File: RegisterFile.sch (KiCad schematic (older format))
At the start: 8 parts, among them U44 IDT71342LA20JG, U45 IDT71342LA20JG, U46 IDT71342LA20JG, U47 IDT71342LA20JG

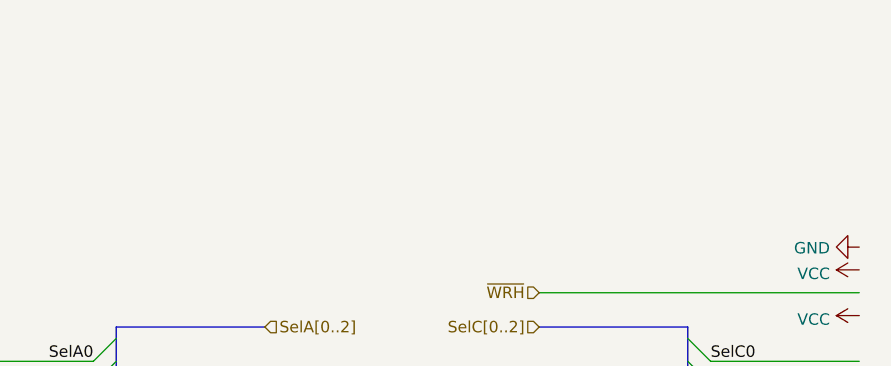
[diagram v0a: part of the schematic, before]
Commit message: Latch the A and B values between ID and EX stages.
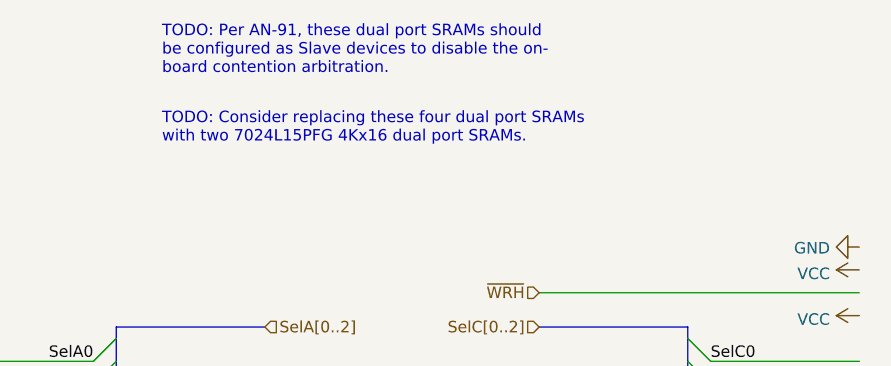
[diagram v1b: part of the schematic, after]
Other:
- note added: "TODO: Consider replacing these four dual port SRAMs\nwith two 7024L15PFG 4Kx16 dual port SRAMs."
- note added: "TODO: Per AN-91, these dual port SRAMs should\nbe configured as Slave devices to disable the on-\nboard contention arbitration."
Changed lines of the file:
@@
 $Descr A2 23386 16535
 encoding utf-8
-Sheet 5 32
+Sheet 4 34
 Title "Register File"
 Date ""
@@
 Text Label 12200 7300 0    50   ~ 0
 C15
+Text Notes 10200 4050 0    50   ~ 0
+TODO: Per AN-91, these dual port SRAMs should\nbe configured as Slave devices to disable the on-\nboard contention arbitration.
+Text Notes 10200 4350 0    50   ~ 0
+TODO: Consider replacing these four dual port SRAMs\nwith two 7024L15PFG 4Kx16 dual port SRAMs.
 Wire Bus Line
 	7100 5150 7100 5400

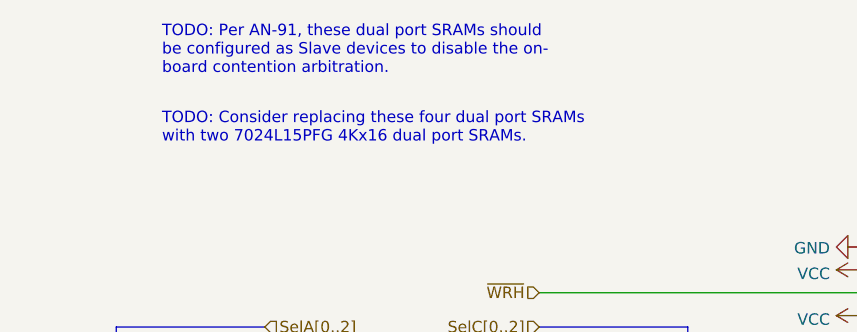
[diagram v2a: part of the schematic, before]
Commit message: Instruction Memory RAM ICs are slave devices.
Per AN-91, the dual port SRAMs in IF should be configured as Slave devices
to disable the on-board contention arbitration. We accept invalid results
during simultaneous access to individual memory cells in return for the
simplicity of not needing to handle the busy signal.
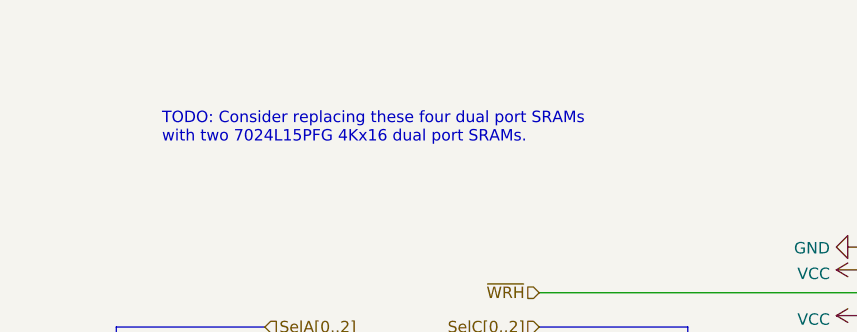
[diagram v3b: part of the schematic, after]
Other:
- note removed: "TODO: Per AN-91, these dual port SRAMs should\nbe configured as Slave devices to disable the on-\nboard contention arbitration."
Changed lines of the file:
@@
 Text Label 12200 7300 0    50   ~ 0
 C15
-Text Notes 10200 4050 0    50   ~ 0
-TODO: Per AN-91, these dual port SRAMs should\nbe configured as Slave devices to disable the on-\nboard contention arbitration.
 Text Notes 10200 4350 0    50   ~ 0
 TODO: Consider replacing these four dual port SRAMs\nwith two 7024L15PFG 4Kx16 dual port SRAMs.

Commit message: Use IDT 7024L15PFG dual port SRAM for the register file.
These are smaller and faster than the ICs I was using before, and I only
need two of them.
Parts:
- removed C50, C51: 100nF, Capacitor_SMD:C_0603_1608Metric_Pad1.08x0.95mm_HandSolder, symbol Device:C
- removed U44, U45, U46, U47: IDT71342LA20JG, Package_LCC:PLCC-52_SMD-Socket, symbol MainBoard-rescue:IDT71342LA20JG-Memory_RAM
- added U10, U9: IDT7024L15PFG, Package_QFP:TQFP-100_14x14mm_P0.5mm, symbol Memory_RAM:IDT7024L15PFG
- renumbered C48 to C14, C49 to C15
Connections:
- wire segments 102 -> 118
- no-connect marks 0 -> 4
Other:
- note added: "Both dual port SRAMs are configured in Slave mode. This disables the\non board contention arbitration logic. Per application note, AN-91, a\nsimultaneous read and write to the same cell will flow through from one\nport to another after a short delay."
- note removed: "TODO: Consider replacing these four dual port SRAMs\nwith two 7024L15PFG 4Kx16 dual port SRAMs."
- moved on the sheet: C14, C15

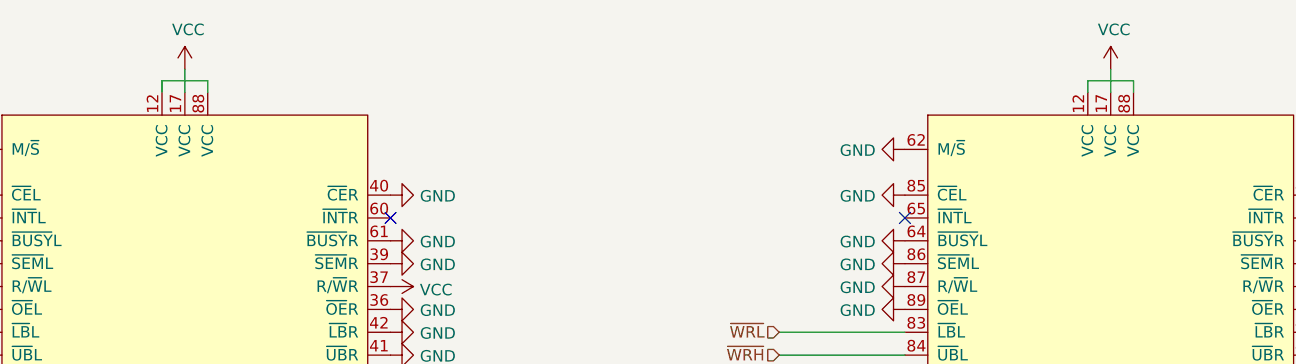
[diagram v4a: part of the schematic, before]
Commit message: Fix ERC errors and change operands in EX.
Now, A is the left operand and B is the right operand. The immediate
value may be selected for the right hand operand.
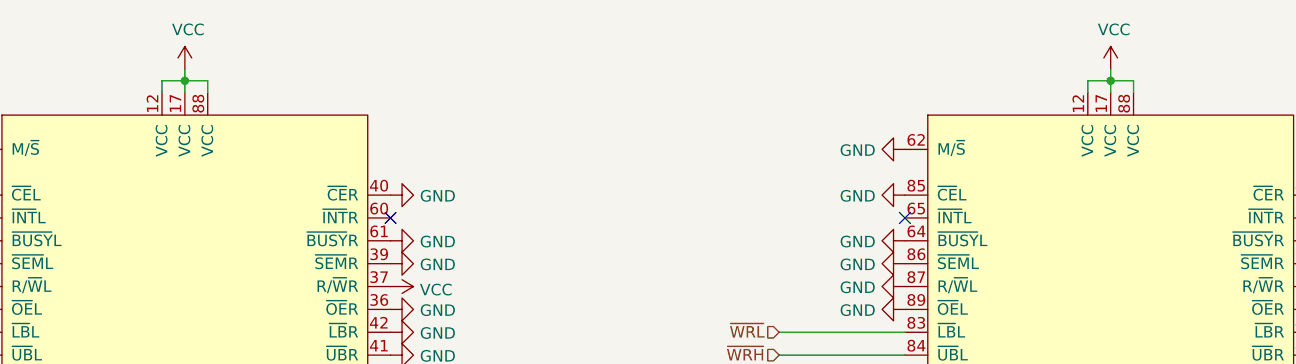
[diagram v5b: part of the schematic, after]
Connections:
- net VCC: now also U10.12 (VCC), U10.88 (VCC), U9.12 (VCC), U9.88 (VCC)
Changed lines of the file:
@@
 $EndComp
 Wire Wire Line
-	3350 1650 3350 1600
-Wire Wire Line
-	3350 1600 3550 1600
+	3350 1600 3450 1600
 Wire Wire Line
 	3550 1600 3550 1650
-Wire Wire Line
-	3450 1650 3450 1550
 $Comp
 L power:VCC #PWR062
@@
 $EndComp
 Wire Wire Line
-	7400 1650 7400 1600
-Wire Wire Line
-	7400 1600 7600 1600
+	7400 1600 7500 1600
 Wire Wire Line
 	7600 1600 7600 1650
-Wire Wire Line
-	7500 1650 7500 1550
 $Comp
 L power:VCC #PWR095
@@
 	0    -1   1    0
 $EndComp
-Wire Bus Line
-	2150 2900 2150 3100
-Wire Bus Line
-	4750 2900 4750 3100
-Wire Bus Line
-	6200 2900 6200 3100
-Wire Bus Line
-	8800 2900 8800 3100
-Wire Bus Line
-	2150 4200 2150 5700
-Wire Bus Line
-	4750 4200 4750 5700
-Wire Bus Line
-	6200 4200 6200 5700
-Wire Bus Line
-	8800 4200 8800 5700
 Text Notes 2550 7250 0    50   ~ 0
 Both dual port SRAMs are configured in Slave mode. This disables the\non board contention arbitration logic. Per application note, AN-91, a\nsimultaneous read and write to the same cell will flow through from one\nport to another after a short delay.
+Wire Wire Line
+	3350 1650 3350 1600
+Wire Wire Line
+	7400 1650 7400 1600
+Wire Wire Line
+	7500 1550 7500 1600
+Connection ~ 7500 1600
+Wire Wire Line
+	7500 1600 7600 1600
+Wire Wire Line
+	7500 1600 7500 1650
+Wire Wire Line
+	3450 1550 3450 1600
+Connection ~ 3450 1600
+Wire Wire Line
+	3450 1600 3550 1600
+Wire Wire Line
+	3450 1600 3450 1650
+Wire Bus Line
+	2150 2900 2150 3100
+Wire Bus Line
+	4750 2900 4750 3100
+Wire Bus Line
+	6200 2900 6200 3100
+Wire Bus Line
+	8800 2900 8800 3100
+Wire Bus Line
+	2150 4200 2150 5700
+Wire Bus Line
+	4750 4200 4750 5700
+Wire Bus Line
+	6200 4200 6200 5700
+Wire Bus Line
+	8800 4200 8800 5700
 $EndSCHEMATC

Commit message: Add a "Mouser" field to components with a link to buy the part.
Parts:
- C14, C15: Mouser (none) -> https://www.mouser.com/ProductDetail/963-EMK107B7104KAHT
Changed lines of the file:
@@
 F 2 "Capacitor_SMD:C_0603_1608Metric_Pad1.08x0.95mm_HandSolder" H 1288 7300 50  0001 C CNN
 F 3 "~" H 1250 7450 50  0001 C CNN
+F 4 "https://www.mouser.com/ProductDetail/963-EMK107B7104KAHT" H 1250 7450 50  0001 C CNN "Mouser"
 	1    1250 7450
 	1    0    0    -1
@@
 F 2 "Capacitor_SMD:C_0603_1608Metric_Pad1.08x0.95mm_HandSolder" H 788 7300 50  0001 C CNN
 F 3 "~" H 750 7450 50  0001 C CNN
+F 4 "https://www.mouser.com/ProductDetail/963-EMK107B7104KAHT" H 750 7450 50  0001 C CNN "Mouser"
 	1    750  7450
 	1    0    0    -1

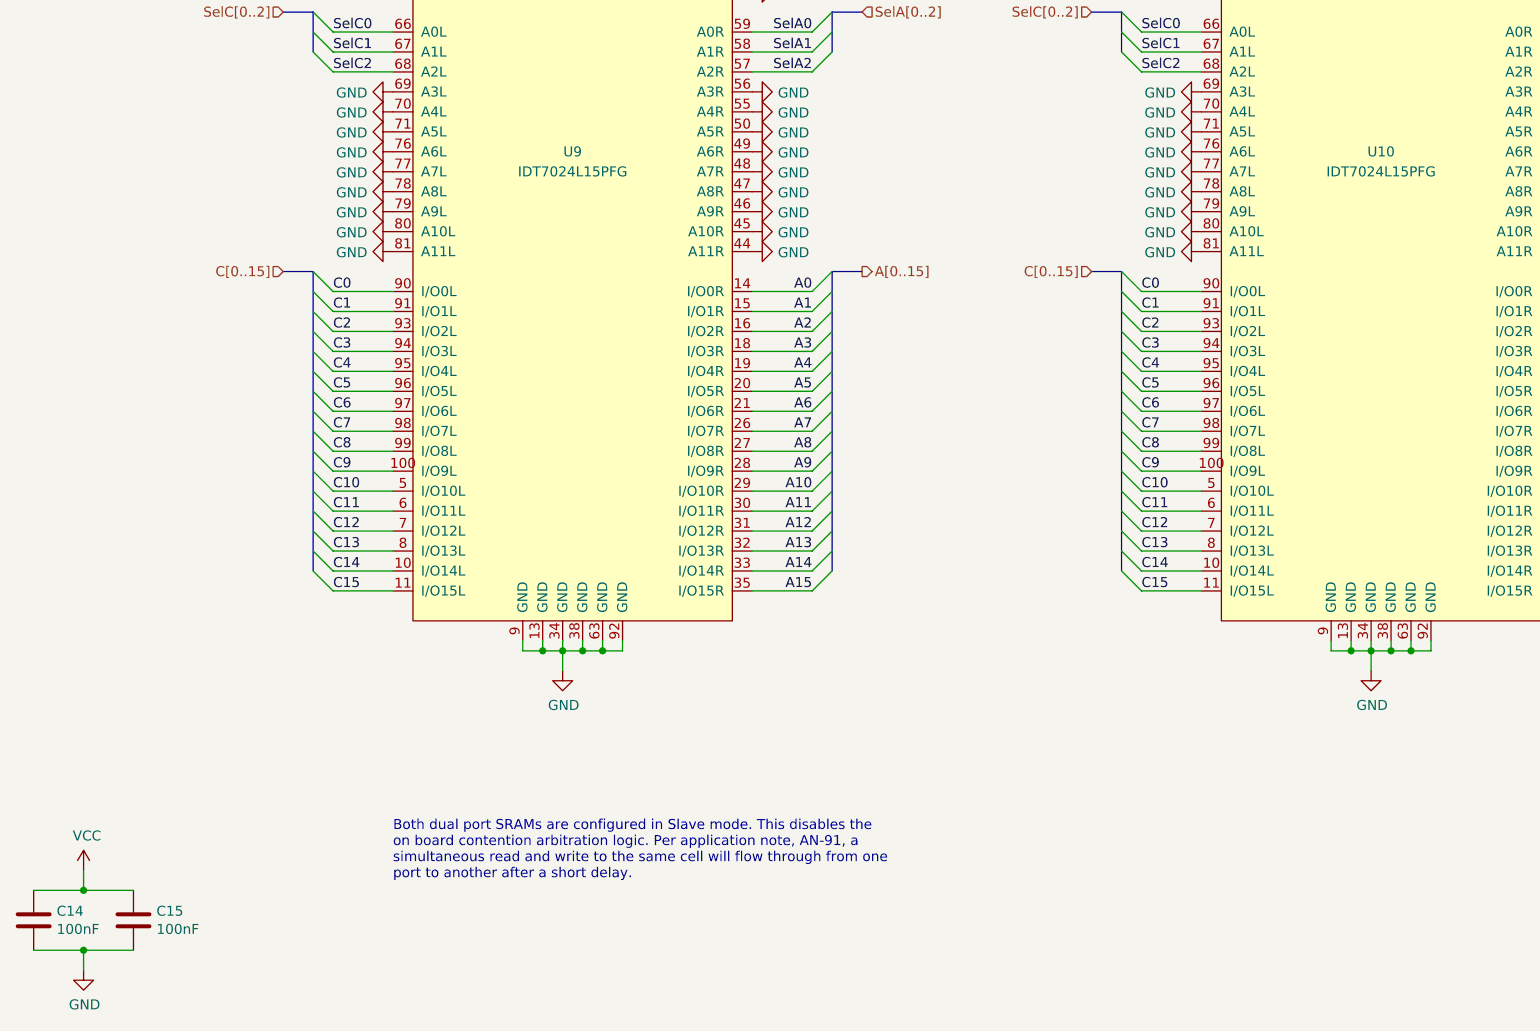
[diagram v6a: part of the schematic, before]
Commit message: Buffer the clock signals and distribute so as to minimize trace length and capacitance.
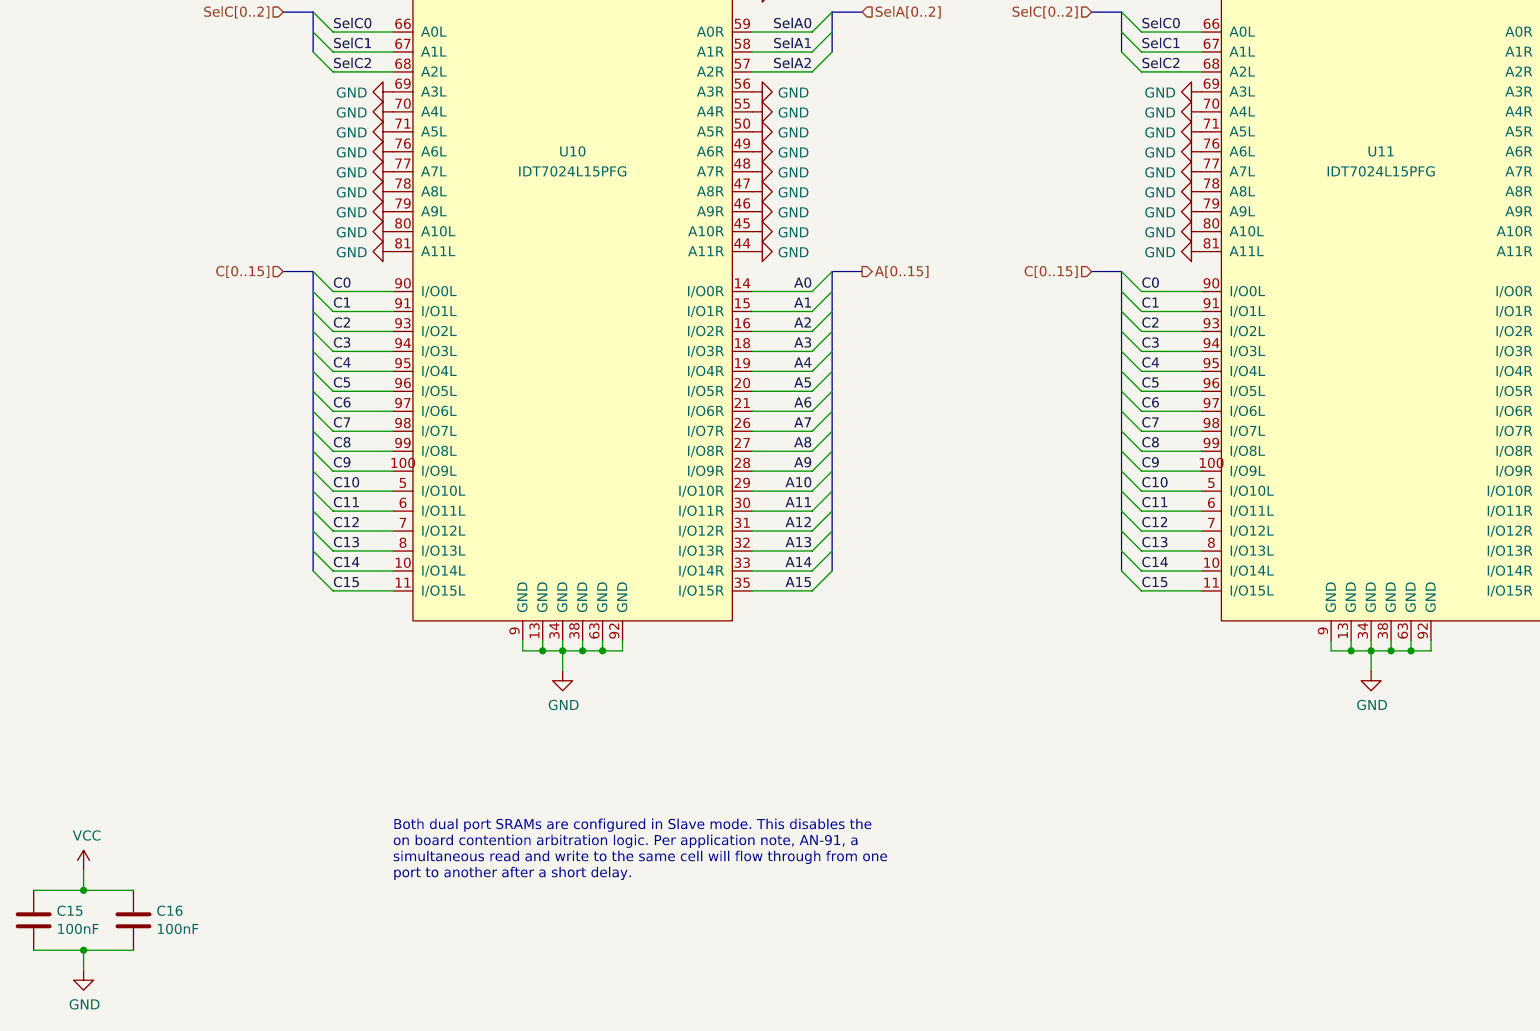
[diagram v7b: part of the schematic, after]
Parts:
- renumbered C14 to C15, C15 to C16, U9 to U10, U10 to U11

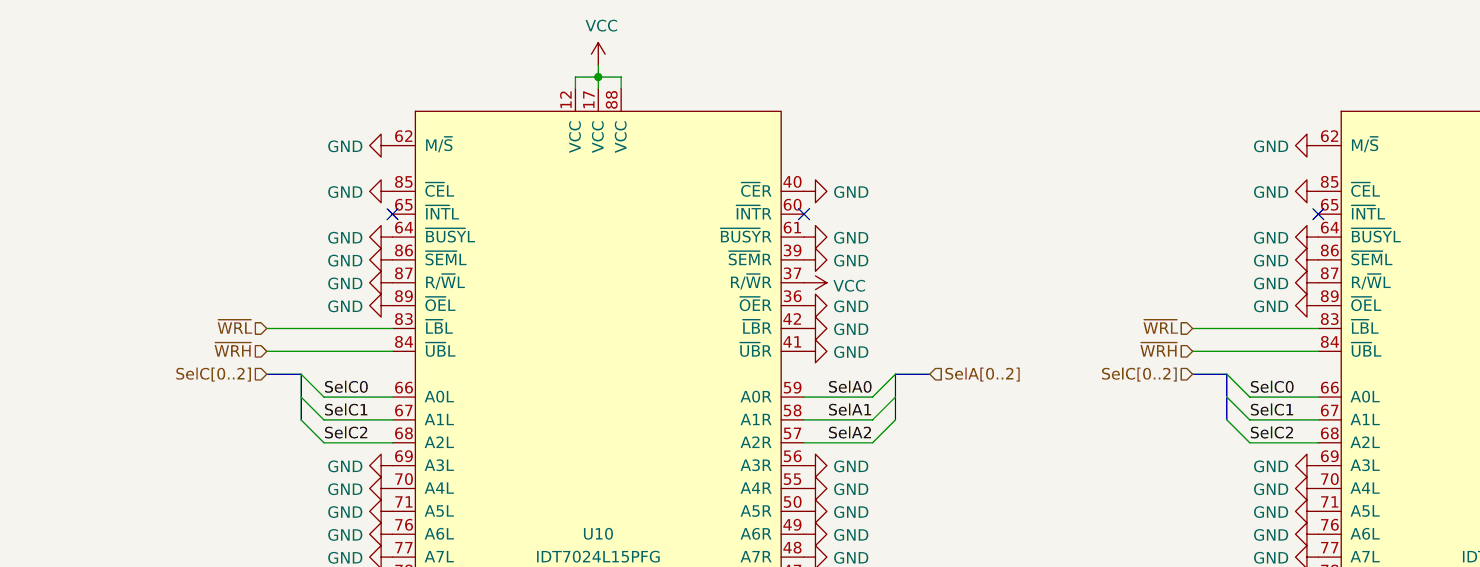
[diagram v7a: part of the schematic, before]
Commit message: Add a new control signal /WBEN.
This controls whether the instruction writes a value back to the register
file at all. This signal works in conjunction with /WRL and /WRH which mask
the lower and upper portions of the word, respectively, during write-back.
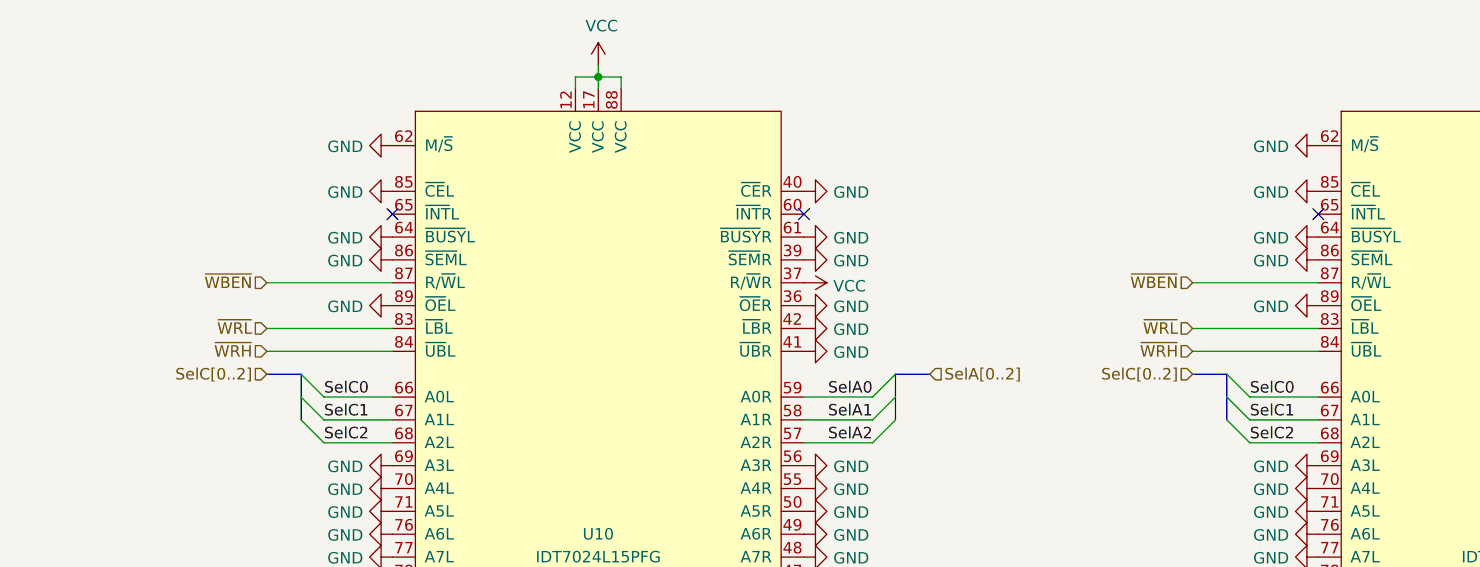
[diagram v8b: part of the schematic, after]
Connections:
- net GND: no longer U10.87 (R/~W~L), U11.87 (R/~W~L)
- new net ~WBEN: U10.87 (R/~W~L), U11.87 (R/~W~L)
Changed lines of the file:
@@
-$EndComp
-$Comp
-L power:GND #PWR054
-U 1 1 5FD4CB2D
-P 2550 2500
-F 0 "#PWR054" H 2550 2250 50  0001 C CNN
-F 1 "GND" V 2555 2372 50  0000 R CNN
-F 2 "" H 2550 2500 50  0001 C CNN
-F 3 "" H 2550 2500 50  0001 C CNN
-	1    2550 2500
-	0    1    1    0
 $EndComp
 $Comp
@@
 $EndComp
 $Comp
-L power:GND #PWR087
-U 1 1 5FDF3587
-P 6600 2500
-F 0 "#PWR087" H 6600 2250 50  0001 C CNN
-F 1 "GND" V 6605 2372 50  0000 R CNN
-F 2 "" H 6600 2500 50  0001 C CNN
-F 3 "" H 6600 2500 50  0001 C CNN
-	1    6600 2500
-	0    1    1    0
-$EndComp
-$Comp
 L power:GND #PWR0100
 U 1 1 5FDF358D
@@
 Wire Wire Line
 	3450 1600 3450 1650
+Text HLabel 2000 2500 0    50   Input ~ 0
+~WBEN
+Wire Wire Line
+	2550 2500 2000 2500
+Text HLabel 6050 2500 0    50   Input ~ 0
+~WBEN
+Wire Wire Line
+	6600 2500 6050 2500
 Wire Bus Line
 	2150 2900 2150 3100
